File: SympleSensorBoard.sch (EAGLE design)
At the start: 45 parts, among them IC1 STM32F303K8T6, SW1 B2B-XH-A_LF__SN_, SW2 B2B-XH-A_LF__SN_, SW3 B2B-XH-A_LF__SN_, SW4 B2B-XH-A_LF__SN_, SW5 B2B-XH-A_LF__SN_, SW6 B2B-XH-A_LF__SN_, SW7 B2B-XH-A_LF__SN_, Y1 CSTCE12M0G55-R0

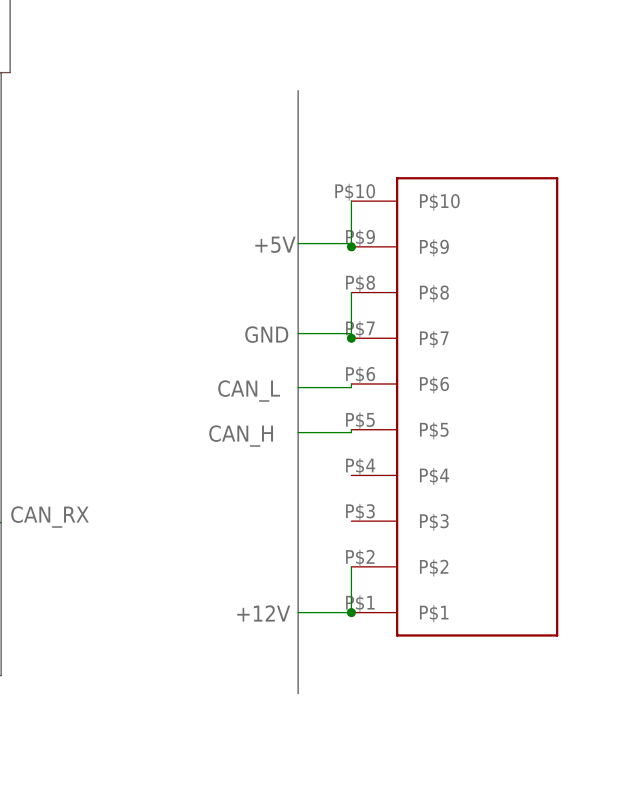
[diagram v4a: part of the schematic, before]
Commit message: 10ピンコネクタのホールの大きさを修正した
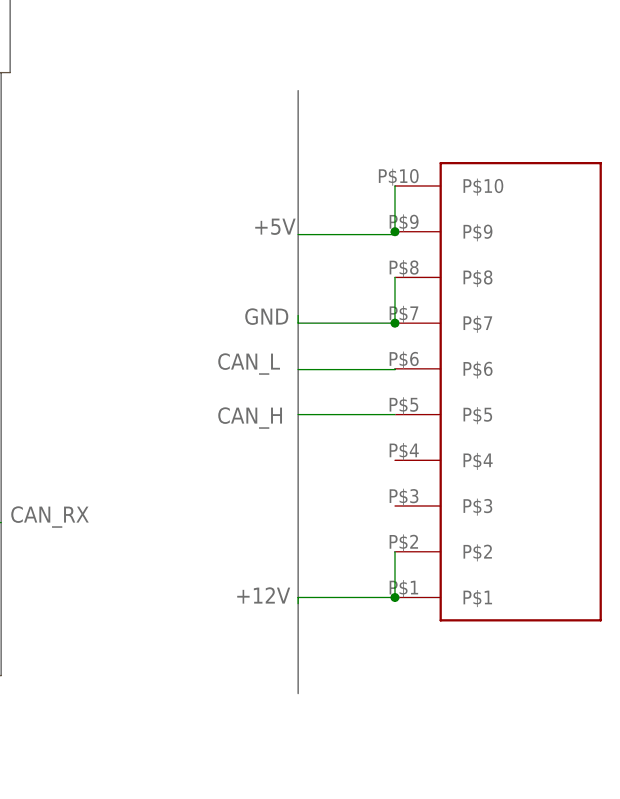
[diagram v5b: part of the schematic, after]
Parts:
- removed BOX10P-L1: BOX10PBOX10P-L, user_conector:BOX10PBOX10P-L
- added U$4: BOX10PBOX10P-L, user_conector:BOX10PBOX10P-L
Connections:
- net +12V: now also U$4.P$1, U$4.P$2; no longer BOX10P-L1.P$1, BOX10P-L1.P$2
- net +5V: now also U$4.P$10, U$4.P$9; no longer BOX10P-L1.P$10, BOX10P-L1.P$9
- net CAN_H: now also U$4.P$5; no longer BOX10P-L1.P$5
- net CAN_L: now also U$4.P$6; no longer BOX10P-L1.P$6
- net GND: now also U$4.P$7, U$4.P$8; no longer BOX10P-L1.P$7, BOX10P-L1.P$8
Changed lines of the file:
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@@
 <setting verticaltext="up"/>
 </settings>
-<grid distance="1" unitdist="mm" unit="mm" style="lines" multiple="1" display="yes" altdistance="0.01" altunitdist="inch" altunit="inch"/>
+<grid distance="1" unitdist="mm" unit="mm" style="lines" multiple="1" display="yes" altdistance="0.01" altunitdist="inch" altunit="mm"/>
 <layers>
 <layer number="1" name="Top" color="4" fill="1" visible="no" active="no"/>
@@
 <part name="R5" library="rcl" library_urn="urn:adsk.eagle:library:334" deviceset="R-US_" device="R0603" package3d_urn="urn:adsk.eagle:package:23555/3" value="150"/>
 <part name="U$3" library="user_conector" deviceset="BOX14P" device=""/>
-<part name="BOX10P-L1" library="user_conector" deviceset="BOX10P" device="BOX10P-L"/>
 <part name="SW1" library="B2B-XH-A_LF__SN_" deviceset="B2B-XH-A_LF__SN_" device=""/>
 <part name="ADC_1" library="B3B-XH-A_LF__SN_" deviceset="B3B-XH-A_LF__SN_" device=""/>
@@
 <part name="SW6" library="B2B-XH-A_LF__SN_" deviceset="B2B-XH-A_LF__SN_" device=""/>
 <part name="SW7" library="B2B-XH-A_LF__SN_" deviceset="B2B-XH-A_LF__SN_" device=""/>
+<part name="U$4" library="user_conector" deviceset="BOX10P" device="BOX10P-L"/>
 </parts>
 <sheets>
@@
 </instance>
 <instance part="U$3" gate="G$1" x="159" y="58" smashed="yes"/>
-<instance part="BOX10P-L1" gate="G$1" x="151" y="-52" smashed="yes" rot="R180"/>
 <instance part="SW1" gate="G$1" x="120" y="-101" smashed="yes">
 <attribute name="NAME" x="136.51" y="-93.38" size="1.778" layer="95" align="center-left"/>
@@
 <attribute name="VALUE" x="136.51" y="-186.92" size="1.778" layer="96" align="center-left"/>
 </instance>
+<instance part="U$4" gate="G$1" x="166" y="-30" smashed="yes" rot="R180"/>
 </instances>
 <busses>
@@
 </segment>
 <segment>
-<pinref part="BOX10P-L1" gate="G$1" pin="P$7"/>
-<pinref part="BOX10P-L1" gate="G$1" pin="P$8"/>
-<wire x1="145.92" y1="-21.52" x2="145.92" y2="-16.44" width="0.1524" layer="91"/>
-<wire x1="140" y1="-21" x2="145.92" y2="-21" width="0.1524" layer="91"/>
-<wire x1="145.92" y1="-21" x2="145.92" y2="-21.52" width="0.1524" layer="91"/>
-<junction x="145.92" y="-21.52"/>
-<label x="134" y="-22" size="1.778" layer="95"/>
-</segment>
-<segment>
 <pinref part="ADC_1" gate="G$1" pin="2"/>
 <wire x1="39" y1="-90.54" x2="15" y2="-90.54" width="0.1524" layer="91"/>
@@
 <wire x1="15" y1="-206.54" x2="15" y2="-207" width="0.1524" layer="91"/>
 <label x="9" y="-207" size="1.778" layer="95"/>
+</segment>
+<segment>
+<pinref part="U$4" gate="G$1" pin="P$7"/>
+<wire x1="150.76" y1="-19.84" x2="140" y2="-19.84" width="0.1524" layer="91"/>
+<wire x1="140" y1="-19.84" x2="140" y2="-19" width="0.1524" layer="91"/>
+<pinref part="U$4" gate="G$1" pin="P$8"/>
+<wire x1="150.76" y1="-14.76" x2="150.76" y2="-19.84" width="0.1524" layer="91"/>
+<junction x="150.76" y="-19.84"/>
+<label x="134" y="-20" size="1.778" layer="95"/>
 </segment>
 </net>
@@
 </segment>
 <segment>
-<pinref part="BOX10P-L1" gate="G$1" pin="P$2"/>
-<pinref part="BOX10P-L1" gate="G$1" pin="P$1"/>
-<wire x1="145.92" y1="-46.92" x2="145.92" y2="-52" width="0.1524" layer="91"/>
-<wire x1="140" y1="-52" x2="145.92" y2="-52" width="0.1524" layer="91"/>
-<junction x="145.92" y="-52"/>
-<label x="133" y="-53" size="1.778" layer="95"/>
+<pinref part="U$4" gate="G$1" pin="P$1"/>
+<wire x1="150.76" y1="-50.32" x2="140" y2="-50.32" width="0.1524" layer="91"/>
+<wire x1="140" y1="-50.32" x2="140" y2="-51" width="0.1524" layer="91"/>
+<pinref part="U$4" gate="G$1" pin="P$2"/>
+<wire x1="150.76" y1="-50.32" x2="150.76" y2="-45.24" width="0.1524" layer="91"/>
+<junction x="150.76" y="-50.32"/>
+<label x="133" y="-51" size="1.778" layer="95"/>
 </segment>
 </net>
@@
 </segment>
 <segment>
-<pinref part="BOX10P-L1" gate="G$1" pin="P$10"/>
-<pinref part="BOX10P-L1" gate="G$1" pin="P$9"/>
-<wire x1="145.92" y1="-6.28" x2="145.92" y2="-11.36" width="0.1524" layer="91"/>
-<wire x1="140" y1="-11" x2="145.92" y2="-11" width="0.1524" layer="91"/>
-<wire x1="145.92" y1="-11" x2="145.92" y2="-11.36" width="0.1524" layer="91"/>
-<junction x="145.92" y="-11.36"/>
-<label x="135" y="-12" size="1.778" layer="95"/>
-</segment>
-<segment>
 <pinref part="ADC_1" gate="G$1" pin="1"/>
 <wire x1="15" y1="-88" x2="39" y2="-88" width="0.1524" layer="91"/>
@@
 <wire x1="39" y1="-204" x2="15" y2="-204" width="0.1524" layer="91"/>
 <label x="10" y="-205" size="1.778" layer="95"/>
+</segment>
+<segment>
+<pinref part="U$4" gate="G$1" pin="P$10"/>
+<pinref part="U$4" gate="G$1" pin="P$9"/>
+<wire x1="150.76" y1="-4.6" x2="150.76" y2="-9.68" width="0.1524" layer="91"/>
+<wire x1="140" y1="-10" x2="150.76" y2="-10" width="0.1524" layer="91"/>
+<wire x1="150.76" y1="-10" x2="150.76" y2="-9.68" width="0.1524" layer="91"/>
+<junction x="150.76" y="-9.68"/>
+<label x="135" y="-10" size="1.778" layer="95"/>
 </segment>
 </net>
@@
 </segment>
 <segment>
-<pinref part="BOX10P-L1" gate="G$1" pin="P$5"/>
-<wire x1="140" y1="-32" x2="145.92" y2="-32" width="0.1524" layer="91"/>
-<wire x1="145.92" y1="-32" x2="145.92" y2="-31.68" width="0.1524" layer="91"/>
-<label x="130" y="-33" size="1.778" layer="95"/>
+<pinref part="U$4" gate="G$1" pin="P$5"/>
+<wire x1="150.76" y1="-30" x2="140" y2="-30" width="0.1524" layer="91"/>
+<label x="131" y="-31" size="1.778" layer="95"/>
 </segment>
 </net>
@@
 </segment>
 <segment>
-<pinref part="BOX10P-L1" gate="G$1" pin="P$6"/>
-<wire x1="140" y1="-27" x2="145.92" y2="-27" width="0.1524" layer="91"/>
-<wire x1="145.92" y1="-27" x2="145.92" y2="-26.6" width="0.1524" layer="91"/>
-<label x="131" y="-28" size="1.778" layer="95"/>
-</segment>
-</net>
+<pinref part="U$4" gate="G$1" pin="P$6"/>
+<wire x1="150.76" y1="-24.92" x2="150.76" y2="-25" width="0.1524" layer="91"/>
+<wire x1="150.76" y1="-25" x2="140" y2="-25" width="0.1524" layer="91"/>
+<label x="131" y="-25" size="1.778" layer="95"/>
+</segment>
+</net>
